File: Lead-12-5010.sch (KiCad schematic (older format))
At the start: 59 parts, among them U1 TL082, U2 TL082

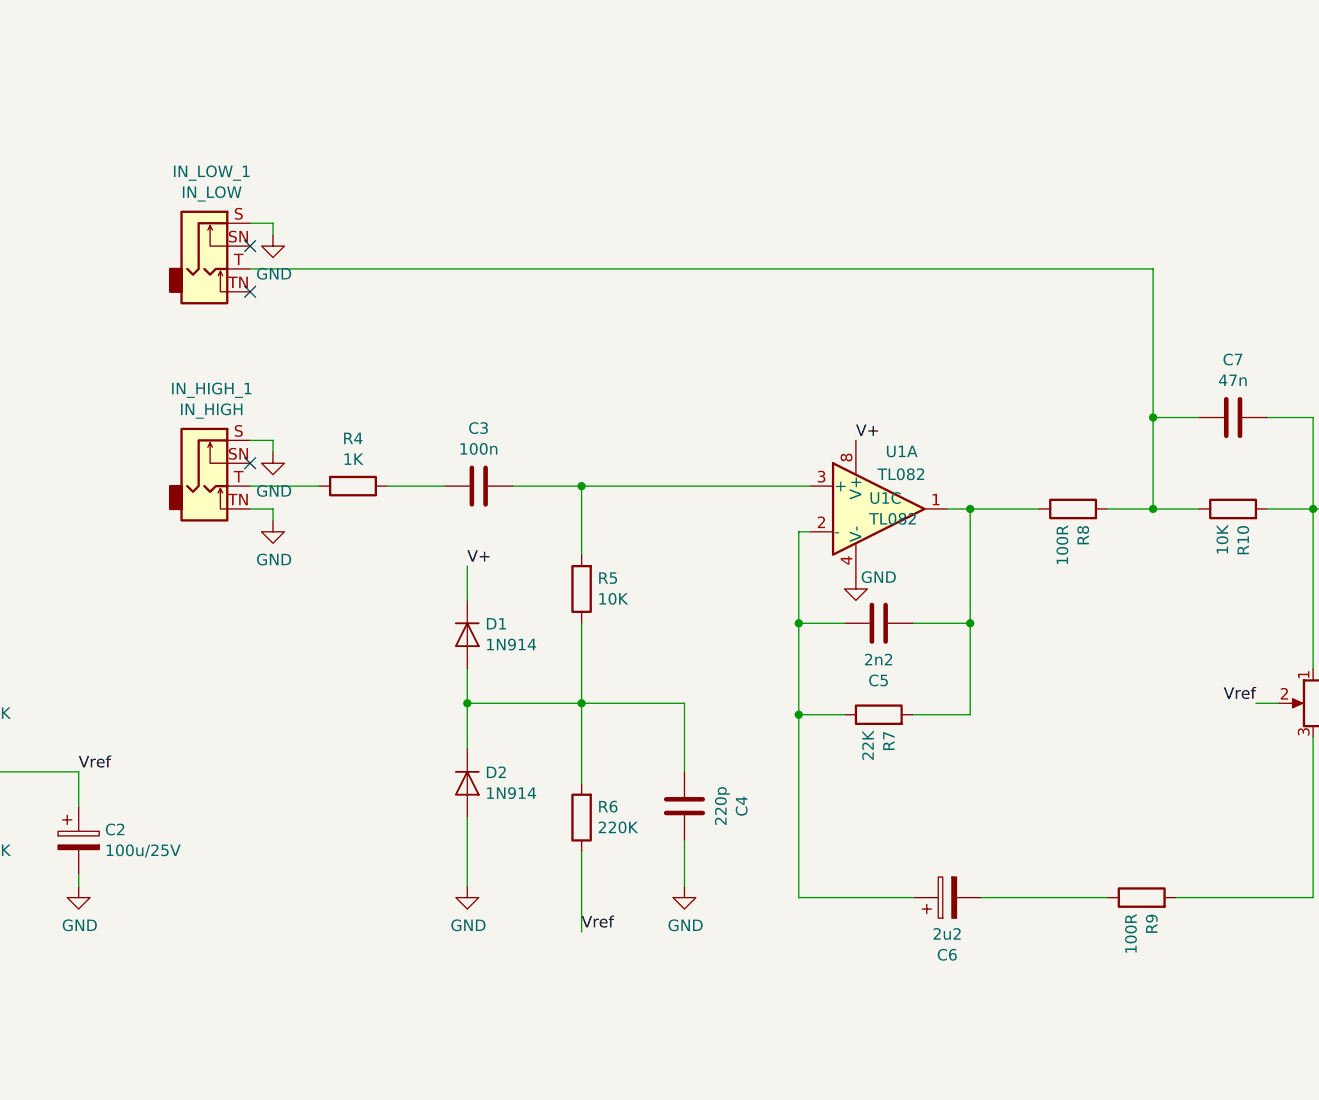
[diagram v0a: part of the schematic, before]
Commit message: Removed low input
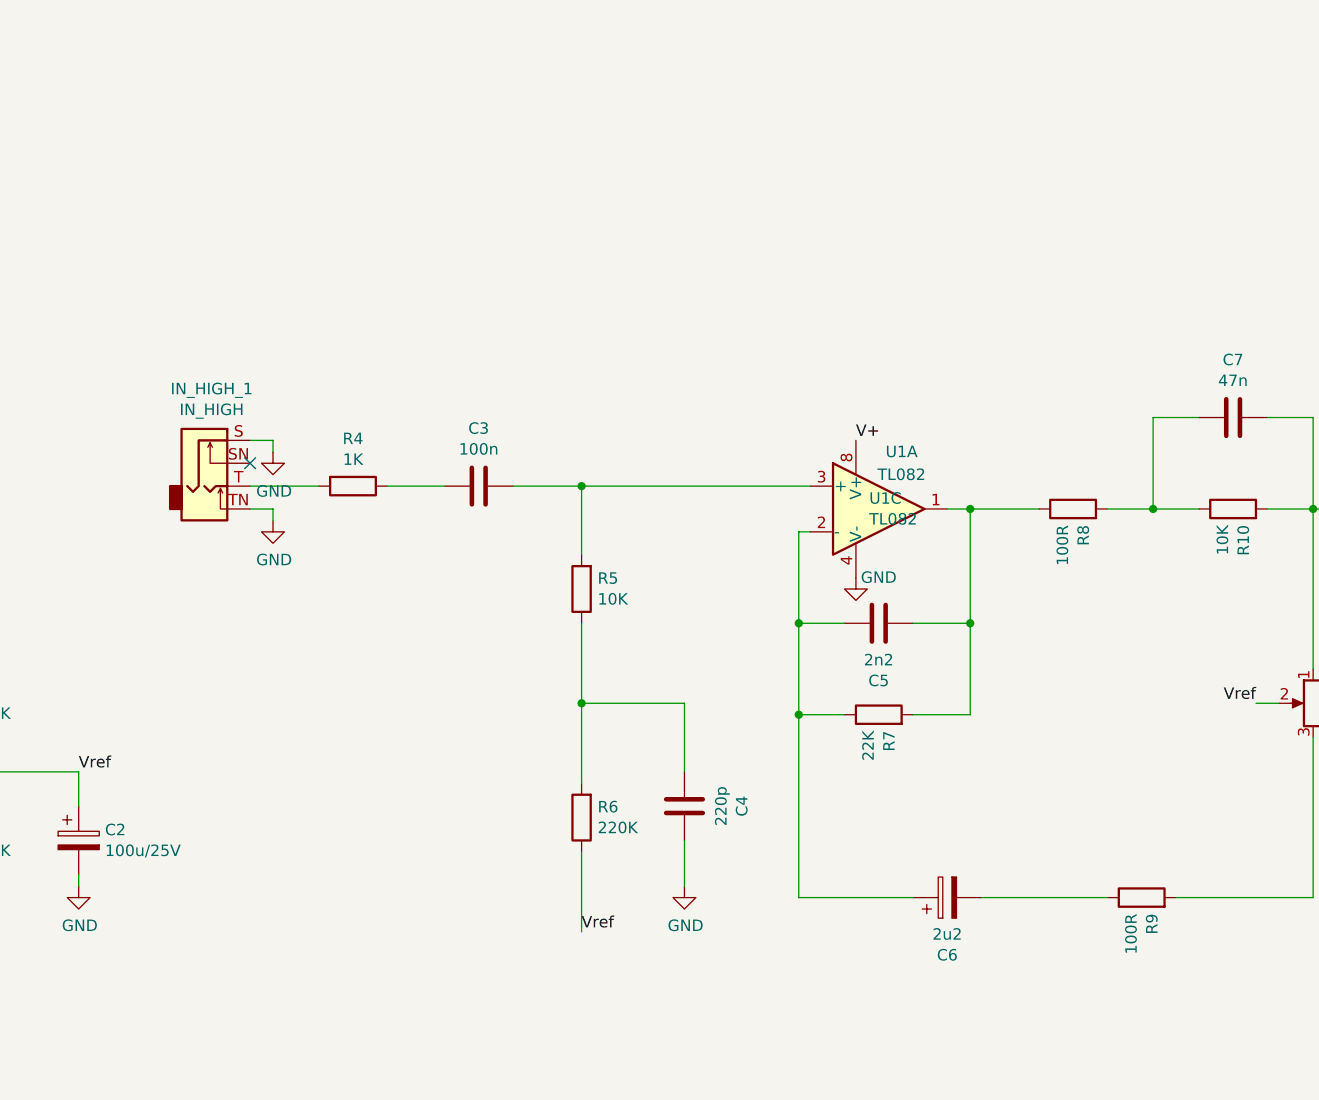
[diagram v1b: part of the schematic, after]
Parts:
- removed D1, D2: 1N914, Diode_THT:D_DO-35_SOD27_P7.62mm_Horizontal, symbol Diode:1N914
- removed IN_LOW_1: IN_LOW, Audio Jacks:6.35MM_STEREO_SWITCHED_JACK, symbol Connector:AudioJack2_Switch
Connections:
- no-connect marks 6 -> 4
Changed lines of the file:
@@
 encoding utf-8
 Sheet 1 1
-Title "JCM800 5W"
+Title "Master Lead 5010 Preamp"
 Date ""
-Rev "0.3"
+Rev "0.2"
 Comp "Dazz"
 Comment1 ""
@@
 $EndComp
 Wire Wire Line
-	8000 3850 8000 4500
-Connection ~ 8000 4500
-$Comp
-L Diode:1N914 D2
-U 1 1 5E630052
-P 5000 6100
-F 0 "D2" V 4954 6179 50  0000 L CNN
-F 1 "1N914" V 5045 6179 50  0000 L CNN
-F 2 "Diode_THT:D_DO-35_SOD27_P7.62mm_Horizontal" H 5000 5925 50  0001 C CNN
-F 3 "http://www.vishay.com/docs/85622/1n914.pdf" H 5000 6100 50  0001 C CNN
-	1    5000 6100
-	0    1    1    0
-$EndComp
-$Comp
-L Diode:1N914 D1
-U 1 1 5E63180D
-P 5000 5450
-F 0 "D1" V 4954 5529 50  0000 L CNN
-F 1 "1N914" V 5045 5529 50  0000 L CNN
-F 2 "Diode_THT:D_DO-35_SOD27_P7.62mm_Horizontal" H 5000 5275 50  0001 C CNN
-F 3 "http://www.vishay.com/docs/85622/1n914.pdf" H 5000 5450 50  0001 C CNN
-	1    5000 5450
-	0    1    1    0
-$EndComp
-Wire Wire Line
-	5000 5950 5000 5750
-$Comp
-L power:GND #PWR09
-U 1 1 5E635F96
-P 5000 6550
-F 0 "#PWR09" H 5000 6300 50  0001 C CNN
-F 1 "GND" H 5005 6377 50  0000 C CNN
-F 2 "" H 5000 6550 50  0001 C CNN
-F 3 "" H 5000 6550 50  0001 C CNN
-	1    5000 6550
-	1    0    0    -1
-$EndComp
-Wire Wire Line
-	5000 6550 5000 6250
-Wire Wire Line
-	5000 5150 5000 5300
-Wire Wire Line
-	5000 5750 5500 5750
-Connection ~ 5000 5750
-Wire Wire Line
-	5000 5750 5000 5600
-Wire Wire Line
 	9850 5000 10300 5000
 Wire Wire Line
@@
 Text Label 1200 5350 0    50   ~ 0
 Vcc
-NoConn ~ 4050 3950
-Wire Wire Line
-	4050 3850 8000 3850
-NoConn ~ 4050 3750
-Wire Wire Line
-	4150 3650 4050 3650
-Wire Wire Line
-	4150 3700 4150 3650
-$Comp
-L power:GND #PWR06
-U 1 1 5E624AE2
-P 4150 3700
-F 0 "#PWR06" H 4150 3450 50  0001 C CNN
-F 1 "GND" H 4155 3527 50  0000 C CNN
-F 2 "" H 4150 3700 50  0001 C CNN
-F 3 "" H 4150 3700 50  0001 C CNN
-	1    4150 3700
-	1    0    0    -1
-$EndComp
-$Comp
-L Connector:AudioJack2_Switch IN_LOW_1
-U 1 1 5E621C5E
-P 3850 3850
-F 0 "IN_LOW_1" H 3882 4275 50  0000 C CNN
-F 1 "IN_LOW" H 3882 4184 50  0000 C CNN
-F 2 "Audio Jacks:6.35MM_STEREO_SWITCHED_JACK" H 3850 4050 50  0001 C CNN
-F 3 "~" H 3850 4050 50  0001 C CNN
-	1    3850 3850
-	1    0    0    -1
-$EndComp
 Wire Wire Line
 	4050 4800 4350 4800
@@
 Text Label 12600 5150 0    50   ~ 0
 V+
-Text Label 5000 5150 0    50   ~ 0
-V+
-$Comp
+$Comp

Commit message: Added filter cap
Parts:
- added C19: 100u/35V, Capacitor_THT:CP_Radial_D8.0mm_P3.50mm, symbol Device:CP
- C1, C2: footprint Capacitor_THT:CP_Radial_D10.0mm_P3.50mm -> Capacitor_THT:CP_Radial_D8.0mm_P3.50mm
- C16: footprint Capacitor_THT:CP_Radial_D8.0mm_P3.50mm -> Capacitor_THT:CP_Radial_D6.3mm_P2.50mm
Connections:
- net GND: now also C19.2
- net at L1.1, R1.2: now also C19.1
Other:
- moved on the sheet: C1, C2, L1, R2, R3
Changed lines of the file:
@@
 L Device:CP C2
 U 1 1 5DC1DA9B
-P 3300 6350
-F 0 "C2" H 3415 6396 50  0000 L CNN
-F 1 "100u/25V" H 3415 6305 50  0000 L CNN
-F 2 "Capacitor_THT:CP_Radial_D10.0mm_P3.50mm" H 3338 6200 50  0001 C CNN
-F 3 "~" H 3300 6350 50  0001 C CNN
-	1    3300 6350
+P 3600 6350
+F 0 "C2" H 3715 6396 50  0000 L CNN
+F 1 "100u/25V" H 3715 6305 50  0000 L CNN
+F 2 "Capacitor_THT:CP_Radial_D8.0mm_P3.50mm" H 3638 6200 50  0001 C CNN
+F 3 "~" H 3600 6350 50  0001 C CNN
+	1    3600 6350
 	1    0    0    -1
 $EndComp
@@
 F 0 "C16" V 13148 5450 50  0000 C CNN
 F 1 "2u2/25V" V 13239 5450 50  0000 C CNN
-F 2 "Capacitor_THT:CP_Radial_D8.0mm_P3.50mm" H 13438 5300 50  0001 C CNN
+F 2 "Capacitor_THT:CP_Radial_D6.3mm_P2.50mm" H 13438 5300 50  0001 C CNN
 F 3 "~" H 13400 5450 50  0001 C CNN
 	1    13400 5450
@@
 L Device:R R2
 U 1 1 5E401592
-P 2800 5750
-F 0 "R2" H 2730 5704 50  0000 R CNN
-F 1 "22K" H 2730 5795 50  0000 R CNN
-F 2 "Resistor_THT:R_Axial_DIN0207_L6.3mm_D2.5mm_P10.16mm_Horizontal" V 2730 5750 50  0001 C CNN
-F 3 "~" H 2800 5750 50  0001 C CNN
-	1    2800 5750
+P 3100 5750
+F 0 "R2" H 3030 5704 50  0000 R CNN
+F 1 "22K" H 3030 5795 50  0000 R CNN
+F 2 "Resistor_THT:R_Axial_DIN0207_L6.3mm_D2.5mm_P10.16mm_Horizontal" V 3030 5750 50  0001 C CNN
+F 3 "~" H 3100 5750 50  0001 C CNN
+	1    3100 5750
 	-1   0    0    1
 $EndComp
@@
 L Device:R R3
 U 1 1 5E401598
-P 2800 6350
-F 0 "R3" H 2730 6304 50  0000 R CNN
-F 1 "22K" H 2730 6395 50  0000 R CNN
-F 2 "Resistor_THT:R_Axial_DIN0207_L6.3mm_D2.5mm_P10.16mm_Horizontal" V 2730 6350 50  0001 C CNN
-F 3 "~" H 2800 6350 50  0001 C CNN
-	1    2800 6350
+P 3100 6350
+F 0 "R3" H 3030 6304 50  0000 R CNN
+F 1 "22K" H 3030 6395 50  0000 R CNN
+F 2 "Resistor_THT:R_Axial_DIN0207_L6.3mm_D2.5mm_P10.16mm_Horizontal" V 3030 6350 50  0001 C CNN
+F 3 "~" H 3100 6350 50  0001 C CNN
+	1    3100 6350
 	-1   0    0    1
 $EndComp
 Wire Wire Line
-	2800 6550 2800 6500
-Wire Wire Line
-	2800 5900 2800 6050
+	3100 6550 3100 6500
+Wire Wire Line
+	3100 5900 3100 6050
 $Comp
 L power:GND #PWR04
 U 1 1 5E41C978
-P 2800 6550
-F 0 "#PWR04" H 2800 6300 50  0001 C CNN
-F 1 "GND" H 2805 6377 50  0000 C CNN
-F 2 "" H 2800 6550 50  0001 C CNN
-F 3 "" H 2800 6550 50  0001 C CNN
-	1    2800 6550
+P 3100 6550
+F 0 "#PWR04" H 3100 6300 50  0001 C CNN
+F 1 "GND" H 3105 6377 50  0000 C CNN
+F 2 "" H 3100 6550 50  0001 C CNN
+F 3 "" H 3100 6550 50  0001 C CNN
+	1    3100 6550
 	1    0    0    -1
 $EndComp
@@
 L power:GND #PWR05
 U 1 1 5E41CD50
-P 3300 6550
-F 0 "#PWR05" H 3300 6300 50  0001 C CNN
-F 1 "GND" H 3305 6377 50  0000 C CNN
-F 2 "" H 3300 6550 50  0001 C CNN
-F 3 "" H 3300 6550 50  0001 C CNN
-	1    3300 6550
-	1    0    0    -1
-$EndComp
-Wire Wire Line
-	3300 6550 3300 6500
-Wire Wire Line
-	3300 6200 3300 6050
-Wire Wire Line
-	3300 6050 2800 6050
-Connection ~ 2800 6050
-Wire Wire Line
-	2800 6050 2800 6200
-Text Label 3300 6050 0    50   ~ 0
+P 3600 6550
+F 0 "#PWR05" H 3600 6300 50  0001 C CNN
+F 1 "GND" H 3605 6377 50  0000 C CNN
+F 2 "" H 3600 6550 50  0001 C CNN
+F 3 "" H 3600 6550 50  0001 C CNN
+	1    3600 6550
+	1    0    0    -1
+$EndComp
+Wire Wire Line
+	3600 6550 3600 6500
+Wire Wire Line
+	3600 6200 3600 6050
+Wire Wire Line
+	3600 6050 3100 6050
+Connection ~ 3100 6050
+Wire Wire Line
+	3100 6050 3100 6200
+Text Label 3600 6050 0    50   ~ 0
 Vref
 $Comp
@@
 L Device:L L1
 U 1 1 5E2BDB5E
-P 1950 5450
-F 0 "L1" V 2140 5450 50  0000 C CNN
-F 1 "5m" V 2049 5450 50  0000 C CNN
-F 2 "Inductor_THT:L_Radial_D6.0mm_P4.00mm" H 1950 5450 50  0001 C CNN
-F 3 "~" H 1950 5450 50  0001 C CNN
-	1    1950 5450
+P 2250 5450
+F 0 "L1" V 2440 5450 50  0000 C CNN
+F 1 "5m" V 2349 5450 50  0000 C CNN
+F 2 "Inductor_THT:L_Radial_D6.0mm_P4.00mm" H 2250 5450 50  0001 C CNN
+F 3 "~" H 2250 5450 50  0001 C CNN
+	1    2250 5450
 	0    -1   -1   0
 $EndComp
-Wire Wire Line
-	1700 5450 1800 5450
 $Comp
 L Device:CP C1
 U 1 1 5E2C99F7
-P 2300 6050
-F 0 "C1" H 2415 6096 50  0000 L CNN
-F 1 "100u/35V" H 2415 6005 50  0000 L CNN
-F 2 "Capacitor_THT:CP_Radial_D10.0mm_P3.50mm" H 2338 5900 50  0001 C CNN
-F 3 "~" H 2300 6050 50  0001 C CNN
-	1    2300 6050
+P 2600 6050
+F 0 "C1" H 2715 6096 50  0000 L CNN
+F 1 "100u/35V" H 2715 6005 50  0000 L CNN
+F 2 "Capacitor_THT:CP_Radial_D8.0mm_P3.50mm" H 2638 5900 50  0001 C CNN
+F 3 "~" H 2600 6050 50  0001 C CNN
+	1    2600 6050
 	-1   0    0    -1
 $EndComp
@@
 L power:GND #PWR03
 U 1 1 5E2C99FD
-P 2300 6550
-F 0 "#PWR03" H 2300 6300 50  0001 C CNN
-F 1 "GND" H 2305 6377 50  0000 C CNN
-F 2 "" H 2300 6550 50  0001 C CNN
-F 3 "" H 2300 6550 50  0001 C CNN
-	1    2300 6550
-	1    0    0    -1
-$EndComp
-Wire Wire Line
-	2300 5450 2300 5900
-Wire Wire Line
-	2300 5450 2800 5450
-Wire Wire Line
-	2800 5450 2800 5600
-Connection ~ 2300 5450
-Wire Wire Line
-	2300 6550 2300 6200
-Text Label 2800 5450 0    50   ~ 0
+P 2600 6550
+F 0 "#PWR03" H 2600 6300 50  0001 C CNN
+F 1 "GND" H 2605 6377 50  0000 C CNN
+F 2 "" H 2600 6550 50  0001 C CNN
+F 3 "" H 2600 6550 50  0001 C CNN
+	1    2600 6550
+	1    0    0    -1
+$EndComp
+Wire Wire Line
+	2600 5450 2600 5900
+Wire Wire Line
+	2600 5450 3100 5450
+Wire Wire Line
+	3100 5450 3100 5600
+Connection ~ 2600 5450
+Wire Wire Line
+	2600 6550 2600 6200
+Text Label 3100 5450 0    50   ~ 0
 V+
 Text Label 6700 4600 0    50   ~ 0
@@
 L power:PWR_FLAG #FLG0101
 U 1 1 5E3BB775
-P 2300 5250
-F 0 "#FLG0101" H 2300 5325 50  0001 C CNN
-F 1 "PWR_FLAG" H 2300 5423 50  0000 C CNN
-F 2 "" H 2300 5250 50  0001 C CNN
-F 3 "~" H 2300 5250 50  0001 C CNN
-	1    2300 5250
-	1    0    0    -1
-$EndComp
-Wire Wire Line
-	2300 5250 2300 5450
-Wire Wire Line
-	2100 5450 2300 5450
+P 2600 5250
+F 0 "#FLG0101" H 2600 5325 50  0001 C CNN
+F 1 "PWR_FLAG" H 2600 5423 50  0000 C CNN
+F 2 "" H 2600 5250 50  0001 C CNN
+F 3 "~" H 2600 5250 50  0001 C CNN
+	1    2600 5250
+	1    0    0    -1
+$EndComp
+Wire Wire Line
+	2600 5250 2600 5450
+Wire Wire Line
+	2400 5450 2600 5450
 $Comp
 L Device:C C18
@@
 Connection ~ 15650 5900
 Connection ~ 15400 5900
+$Comp
+L Device:CP C19
+U 1 1 5E660968
+P 1850 6050
+F 0 "C19" H 1965 6096 50  0000 L CNN
+F 1 "100u/35V" H 1965 6005 50  0000 L CNN
+F 2 "Capacitor_THT:CP_Radial_D8.0mm_P3.50mm" H 1888 5900 50  0001 C CNN
+F 3 "~" H 1850 6050 50  0001 C CNN
+	1    1850 6050
+	-1   0    0    -1
+$EndComp
+$Comp
+L power:GND #PWR0102
+U 1 1 5E66096E
+P 1850 6550
+F 0 "#PWR0102" H 1850 6300 50  0001 C CNN
+F 1 "GND" H 1855 6377 50  0000 C CNN
+F 2 "" H 1850 6550 50  0001 C CNN
+F 3 "" H 1850 6550 50  0001 C CNN
+	1    1850 6550
+	1    0    0    -1
+$EndComp
+Wire Wire Line
+	1850 6550 1850 6200
+Wire Wire Line
+	1700 5450 1850 5450
+Connection ~ 1850 5450
+Wire Wire Line
+	1850 5450 1850 5900
+Wire Wire Line
+	1850 5450 2100 5450
 $EndSCHEMATC

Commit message: Changed output buffer to BJT, removed op amp booster
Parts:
- removed BOOST1: 25K, Potentiometer_THT:Potentiometer_Bourns_3296W_Vertical, symbol Device:R_POT
- removed C14: 47u, Capacitor_THT:CP_Radial_D8.0mm_P3.50mm, symbol Device:CP
- removed C15: 220p, Capacitor_THT:C_Disc_D5.0mm_W2.5mm_P5.00mm, symbol Device:C
- removed R15: 1K, Resistor_THT:R_Axial_DIN0207_L6.3mm_D2.5mm_P10.16mm_Horizontal, symbol Device:R
- removed U2: TL082, Package_DIP:DIP-8_W7.62mm_Socket, symbol Amplifier_Operational:TL082
- added Q1: 2N3904, Package_TO_SOT_THT:TO-92_Inline, symbol Transistor_BJT:2N3904
- added R17: 33k, Resistor_THT:R_Axial_DIN0207_L6.3mm_D2.5mm_P10.16mm_Horizontal, symbol Device:R
- L1: value 5m -> 5mH
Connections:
- net GND: now also R17.2
- net V+: now also Q1.3 (C)
- net at TREBLE1.2: now also Q1.2 (B)
- net at C16.1: now also Q1.1 (E), R17.1
- no-connect marks 4 -> 3
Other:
- moved on the sheet: BASS1, C1, C10, C11, C12, C13, C16, C17, C18, C19, C2, C3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

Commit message: New transistor footprint
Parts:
- Q1: footprint Package_TO_SOT_THT:TO-92_Inline -> Package_TO_SOT_THT:TO-92L_Inline_Wide
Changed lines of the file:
@@
 F 0 "Q1" H 11040 4096 50  0000 L CNN
 F 1 "2N3904" H 11040 4005 50  0000 L CNN
-F 2 "Package_TO_SOT_THT:TO-92_Inline" H 11050 3975 50  0001 L CIN
+F 2 "Package_TO_SOT_THT:TO-92L_Inline_Wide" H 11050 3975 50  0001 L CIN
 F 3 "https://www.fairchildsemi.com/datasheets/2N/2N3904.pdf" H 10850 4050 50  0001 L CNN
 	1    10850 4050

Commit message: Removed low input. Restored output buffer. JST connectors used instead of terminal blocks.
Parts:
- OUT1, Vcc1: footprint TerminalBlock_MetzConnect:TerminalBlock_MetzConnect_Type094_RT03502HBLU_1x02_P5.00mm_Horizontal -> Connector_JST:JST_PH_B2B-PH-K_1x02_P2.00mm_Vertical
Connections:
- net GND: now also OUT1.2 (Pin_2)
- net at C18.1, LEVEL1.2, OUT1.1 (Pin_1): no longer OUT1.2 (Pin_2)
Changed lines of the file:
@@
 	9500 4450 9800 4450
-$Comp
-L Connector:Conn_01x02_Male Vcc1
-U 1 1 5DC75B04
-P 2550 6650
-F 0 "Vcc1" H 2658 6831 50  0000 C CNN
-F 1 "Vcc" H 2658 6740 50  0000 C CNN
-F 2 "TerminalBlock_MetzConnect:TerminalBlock_MetzConnect_Type094_RT03502HBLU_1x02_P5.00mm_Horizontal" H 2550 6650 50  0001 C CNN
-F 3 "~" H 2550 6650 50  0001 C CNN
-	1    2550 6650
-	1    0    0    1
-$EndComp
 $Comp
 L Mechanical:MountingHole H1
@@
 Wire Wire Line
 	6950 7000 6950 7100
-Wire Wire Line
-	2750 6550 2750 6500
 $Comp
 L power:GND #PWR01
 U 1 1 5E5E4B7C
-P 2750 6500
-F 0 "#PWR01" H 2750 6250 50  0001 C CNN
-F 1 "GND" H 2755 6327 50  0000 C CNN
-F 2 "" H 2750 6500 50  0001 C CNN
-F 3 "" H 2750 6500 50  0001 C CNN
-	1    2750 6500
-	-1   0    0    1
+P 2750 6750
+F 0 "#PWR01" H 2750 6500 50  0001 C CNN
+F 1 "GND" H 2755 6577 50  0000 C CNN
+F 2 "" H 2750 6750 50  0001 C CNN
+F 3 "" H 2750 6750 50  0001 C CNN
+	1    2750 6750
+	1    0    0    -1
 $EndComp
 NoConn ~ 9150 5050
@@
 	0    -1   -1   0
 $EndComp
-$Comp
-L Connector:Conn_01x02_Male OUT1
-U 1 1 5E2B9C12
-P 14300 4900
-F 0 "OUT1" H 14408 5081 50  0000 C CNN
-F 1 "OUT" H 14408 4990 50  0000 C CNN
-F 2 "TerminalBlock_MetzConnect:TerminalBlock_MetzConnect_Type094_RT03502HBLU_1x02_P5.00mm_Horizontal" H 14300 4900 50  0001 C CNN
-F 3 "~" H 14300 4900 50  0001 C CNN
-	1    14300 4900
-	-1   0    0    -1
-$EndComp
-Wire Wire Line
-	14100 4900 14100 5000
-Wire Wire Line
-	14100 4900 13850 4900
-Connection ~ 14100 4900
 Connection ~ 13850 4900
 $Comp
@@
 Text GLabel 4850 6650 2    50   Input ~ 0
 V+
+$Comp
+L Connector:Conn_01x02_Male Vcc1
+U 1 1 5F70304A
+P 2550 6650
+F 0 "Vcc1" H 2658 6831 50  0000 C CNN
+F 1 "Vcc" H 2658 6740 50  0000 C CNN
+F 2 "Connector_JST:JST_PH_B2B-PH-K_1x02_P2.00mm_Vertical" H 2550 6650 50  0001 C CNN
+F 3 "~" H 2550 6650 50  0001 C CNN
+	1    2550 6650
+	1    0    0    -1
+$EndComp
+$Comp
+L Connector:Conn_01x02_Male OUT1
+U 1 1 5F720707
+P 14450 4900
+F 0 "OUT1" H 14422 4874 50  0000 R CNN
+F 1 "OUT" H 14422 4783 50  0000 R CNN
+F 2 "Connector_JST:JST_PH_B2B-PH-K_1x02_P2.00mm_Vertical" H 14450 4900 50  0001 C CNN
+F 3 "~" H 14450 4900 50  0001 C CNN
+	1    14450 4900
+	-1   0    0    -1
+$EndComp
+Wire Wire Line
+	13850 4900 14250 4900
+$Comp
+L power:GND #PWR0104
+U 1 1 5F72AB85
+P 14250 5000
+F 0 "#PWR0104" H 14250 4750 50  0001 C CNN
+F 1 "GND" H 14255 4827 50  0000 C CNN
+F 2 "" H 14250 5000 50  0001 C CNN
+F 3 "" H 14250 5000 50  0001 C CNN
+	1    14250 5000
+	1    0    0    -1
+$EndComp
 $EndSCHEMATC
